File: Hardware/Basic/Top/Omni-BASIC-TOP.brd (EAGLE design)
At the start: 38 x 38 mm, 29 parts, among them U2 NRF52832_MODULE_MDBT42

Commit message: commit operation
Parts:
- added C2, C5, C6: 1u, LinnesLab-Passives:C0603
- added C20, C21: 4.7u, LinnesLab-Passives:C0603
- added C22: 100n, LinnesLab-Passives:C0603
- added C23, C24: 47p, LinnesLab-Passives:C0603
- added CHRG2: MCP73831, LinnesLab-Power:SOT23-5
- added D4, D5: (no value), LinnesLab-DiscreteSemi:USC
- added J1: (no value), LinnesLab-Connectors:1X07
- added J2: (no value), LinnesLab-Connectors:1X02
- added JP2: (no value), LinnesLab-Switches:SMT-JUMPER_2_NO_SILK
- added LDO2: MIC5504, LinnesLab-Power:SOT23-5
- added LED5: RED, LinnesLab-LED:LED-0603
- added LED6: YELLOW, LinnesLab-LED:LED-0603
- added R1, R2: 10k, LinnesLab-Passives:R0603
- added R11: (no value), LinnesLab-Passives:R0603
- added R12, R13, R14, R15: 100k, LinnesLab-Passives:R0603
- added R17, R18: 27, LinnesLab-Passives:R0603
- added R19, R20: 1k, LinnesLab-Passives:R0603
- added R21, R22: 0, LinnesLab-Passives:R0603
- added SW1, SW2: SWITCH.MOM, LinnesLab-Switches:TACTILE_SWITCH_SMD_6.2MM_TALL
- added U4: PCF8523, LinnesLab-Clocks:SO8
- added U5: FT231XS, LinnesLab-DigitalIC:SSOP20_L
- added USB2: USB.MICRO-BIGGERPADS, LinnesLab-Connectors:USB-MICRO-01.BIGGERPADS
- added XTAL3: 32.7680kHz, LinnesLab-Clocks:2-SMD.NOLEAD.2.0MMTO1.2MM
- moved SD2 14.5 mm to (20.3, 14.0), flipped to the bottom, turned to 270 degrees
- moved R7 4.58 mm to (6.58, 13.2)
- moved R6 4.58 mm to (6.58, 15.9)
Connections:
- removed net CD1: SD2.CD1
- removed net CS.OLED: U3.13
- removed net DC.OLED: U3.15
- removed net RESET.OLED: U3.14
- removed net RXD: U2.21
- removed net SD.CS: SD2.2
- removed net TXD: U2.19
- new net !CTS: JP2.2, U5.9
- new net !DTR: U5.1
- new net A4/BATTERY_STATUS: R13.1, R14.2, U2.5
- new net A6/TIA: J1.5, U2.7
- new net A7/PPG: J1.7, U2.8
- new net D11/SW1: SW1.A1, U2.25
- new net D15/SW2: SW2.A1, U2.29
- new net D16/CS.OLED: U2.30, U3.13
- new net D27/CHARGE_STATUS: CHRG2.1, R12.1, U2.4
- new net D29/LED.CONTROL: J1.6, U2.6
- new net D3/RESET.OLED: U2.16, U3.14
- new net D4/DC.OLED: U2.17, U3.15
- new net D5/CD1: SD2.CD1, U2.18
- new net D7/SD.CS: SD2.2, U2.20
- new net FT3V3: U5.13
- new net N$17: CHRG2.5, R11.2
- new net N$19: U4.2, XTAL3.P$1
- new net N$20: U4.1, XTAL3.P$2
- new net N$23: R17.2, U5.12
- new net N$24: R18.2, U5.11
- new net N$25: LED5.C, R19.2
- new net N$26: LED6.C, R20.2
- new net RXD.FT: R22.1, U5.4
- new net RXD.NRF: R21.2, U2.21
- new net RXLED: R19.1, U5.17
- new net TXD.FT: R21.1, U5.20
- new net TXD.NRF: R22.2, U2.19
- new net TXLED: R20.1, U5.10
- new net USB+: C23.1, R18.1, USB2.3
- new net USB-: C24.2, R17.1, USB2.2
- new net VBATT: U4.3
- new net VIN: C21.2, C5.2, CHRG2.4, D4.-, D5.-, LDO2.1, LDO2.3, R12.2
- new net VLIPO: C20.1, CHRG2.3, D4.+, J2.2, R13.2
- new net V_USB: D5.+, U5.15, USB2.1
- net 3.3V: now also C2.1, C22.2, C6.1, LDO2.5, LED5.A, LED6.A, R1.2, R15.2, R2.2, U4.8, U5.14, U5.3
- net GND: now also C2.2, C20.2, C21.1, C22.1, C23.2, C24.1, C5.1, C6.2, CHRG2.2, J2.1, JP2.1, LDO2.2, R11.1, R14.1, R15.1, SW1.B1, SW1.B2, SW2.B1, SW2.B2, U4.4, U5.16, U5.6, USB2.5
- net SCL: now also R2.1, U4.6
- net SDA: now also R1.1, U4.5

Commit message: Latest Update
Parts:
- removed C15: 2.2uF, LinnesLab-Passives:C0402
- removed C2, C6, C7: 1u, LinnesLab-Passives:C0603
- removed C22: 100n, LinnesLab-Passives:C0603
- removed C23, C24: 47p, LinnesLab-Passives:C0603
- removed CHRG2: MCP73831, LinnesLab-Power:SOT23-5
- removed CORTEX1: CORTEX_DEBUG_PTH, LinnesLab-Connectors:2X5-PTH-1.27MM
- removed D4, D5: (no value), LinnesLab-DiscreteSemi:USC
- removed JP2: (no value), LinnesLab-Switches:SMT-JUMPER_2_NO_SILK
- removed L2: 10u, LinnesLab-Passives:L0603
- removed LDO2: MIC5504, LinnesLab-Power:SOT23-5
- removed LED5: RED, LinnesLab-LED:LED-0603
- removed LED6: YELLOW, LinnesLab-LED:LED-0603
- removed R19, R20, R3, R4: 1k, LinnesLab-Passives:R0603
- removed R21, R22: 0, LinnesLab-Passives:R0603
- removed R5: 10k, LinnesLab-Passives:R0603
- removed U2: NRF52832_MODULE_MDBT42, LinnesLab-Microcontrollers:BLE_MODULE_RAYTAC_MDBT42
- removed U5: FT231XS, LinnesLab-DigitalIC:SSOP20_L
- removed USB2: USB.MICRO-BIGGERPADS, LinnesLab-Connectors:USB-MICRO-01.BIGGERPADS
- removed XTAL2: 32.768kHz, LinnesLab-Clocks:2-SMD.NOLEAD.2.0MMTO1.2MM
- removed XTAL3: 32.7680kHz, LinnesLab-Clocks:2-SMD.NOLEAD.2.0MMTO1.2MM
- added C3: 1u, LinnesLab-Passives:C0603
- added C4: 10u, LinnesLab-Passives:C0805
- added D2, D3: (no value), LinnesLab-DiscreteSemi:USC
- added DEBUG1: CORTEX_DEBUG_PTH, LinnesLab-Connectors:2X5-PTH-1.27MM
- added JP1: (no value), LinnesLab-Switches:SMT-JUMPER_2_NO_SILK
- added L1: 10u, LinnesLab-Passives:L0603
- added LED1: RED, LinnesLab-LED:LED-0603
- added LED2: BLUE, LinnesLab-LED:LED-0603
- added R10: 10k, LinnesLab-Passives:R0603
- added R16, R8, R9: 1k, LinnesLab-Passives:R0603
- added U1: NRF52832_MODULE_MDBT42, LinnesLab-Microcontrollers:BLE_MODULE_RAYTAC_MDBT42
- added USB1: USB.MICRO-BIGGERPADS, LinnesLab-Connectors:USB-MICRO-01.BIGGERPADS
- added XTAL1: 32.768kHz, LinnesLab-Clocks:2-SMD.NOLEAD.2.0MMTO1.2MM
- C11: value 300p -> 47p
- C12: value 10u -> 100n; device LinnesLab-Passives:C0805 -> LinnesLab-Passives:C0603
- C13: value 2.2uF -> 47p; device LinnesLab-Passives:C0402 -> LinnesLab-Passives:C0603
- C20, C21: value 4.7u -> 2.2uF; device LinnesLab-Passives:C0603 -> LinnesLab-Passives:C0402
- C5: value 1u -> (none)
- C9: value (none) -> 300p
- J1: device LinnesLab-Connectors:1X07 -> LinnesLab-Connectors:1X02
- J2: device LinnesLab-Connectors:1X02 -> LinnesLab-Connectors:1X07_1.27MM
- LED4: value BLUE -> YELLOW
- R11: value (none) -> 27
- R12: value 100k -> 27
- R13: value 100k -> 10k
- R14: value 100k -> 1k
- R15: value 100k -> 390k
- R17, R18: value 27 -> 0
- R6: value 10k -> 100k
- R7: value 390k -> 100k
- SW1, SW2: value SWITCH.MOM -> (none); device LinnesLab-Switches:TACTILE_SWITCH_SMD_6.2MM_TALL -> LinnesLab-Switches:BUTTON-GULLWING
- SW3, SW4: value (none) -> SWITCH.MOM; device LinnesLab-Switches:BUTTON-GULLWING -> LinnesLab-Switches:TACTILE_SWITCH_SMD_6.2MM_TALL
- U3: value (none) -> FT231XS; device LinnesLab-Displays:UG-2864HSWEG01_0.96IN_NO-WRAPAROUND -> LinnesLab-DigitalIC:SSOP20_L
- U4: value PCF8523 -> (none); device LinnesLab-Clocks:SO8 -> LinnesLab-Displays:UG-2864HSWEG01_0.96IN_NO-WRAPAROUND
- moved R2 62.6 mm to (11.5, 36.4)
- moved R1 58.2 mm to (7.89, 36.3)
- moved R18 50.7 mm to (3.51, 11.3)
- moved C14 49.5 mm to (1.62, 9.02)
- moved R17 46.0 mm to (7.56, 11.3)
- moved D1 43.0 mm to (7.55, 3.31), flipped to the bottom, turned to 270 degrees
- moved SW2 38.9 mm to (35.0, 18.5), turned to 180 degrees
- moved LED4 35.0 mm to (13.5, 9.06), turned to 180 degrees
- moved LED3 34.3 mm to (13.5, 7.64), turned to 180 degrees
- moved SW1 32.0 mm to (35.0, 35.8)
- moved SW3 31.2 mm to (32.2, 3.96), turned to 180 degrees
- moved C11 26.1 mm to (12.5, 5.19), turned to 270 degrees
- moved C13 24.3 mm to (12.2, 1.54), turned to 0 degrees
- moved SW4 24.3 mm to (22.5, 3.96)
- moved C5 21.0 mm to (26.4, 19.4), turned to 180 degrees
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- renumbered SD2 to SD1
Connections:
- removed net N$17: CHRG2.5, R11.2
- removed net N$19: U4.2, XTAL3.P$1
- removed net N$20: U4.1, XTAL3.P$2
- removed net VBATT: U4.3
- net !CTS: now also JP1.2, U3.9; no longer JP2.2, U5.9
- net !DTR: now also U3.1; no longer U5.1
- net 3.3V: now also C14.2, C20.2, C21.2, C4.2, D3.-, DEBUG1.1, J2.4, LED3.A, LED4.A, R10.2, U1.11, U3.14, U3.3, U4.6, U4.9; no longer C12.2, C17.2, C19.2, C2.1, C22.2, C6.1, CORTEX1.1, D1.-, LDO2.5, LED5.A, LED6.A, R15.2, R5.2, U2.11, U3.6, U3.9, U4.8, U5.14, U5.3
- net A4/BATTERY_STATUS: now also R6.1, R7.2, U1.5; no longer R13.1, R14.2, U2.5
- net A6/TIA: now also J2.6, U1.7; no longer J1.5, U2.7
- net A7/PPG: now also J2.7, U1.8; no longer J1.7, U2.8
- net D11/SW1: now also SW3.A1, U1.25; no longer SW1.A1, U2.25
- net D15/SW2: now also SW4.A1, U1.29; no longer SW2.A1, U2.29
- net D16/CS.OLED: now also U1.30, U4.13; no longer U2.30, U3.13
- net D27/CHARGE_STATUS: now also U1.4; no longer CHRG2.1, R12.1, U2.4
- net D29/LED.CONTROL: now also J2.5, U1.6; no longer J1.6, U2.6
- net D3/RESET.OLED: now also U1.16, U4.14; no longer U2.16, U3.14
- net D4/DC.OLED: now also U1.17, U4.15; no longer U2.17, U3.15
- net D5/CD1: now also U1.18; no longer U2.18
- net D7/SD.CS: now also U1.20; no longer U2.20
- net DFU: now also SW1.3, U1.34; no longer SW3.3, U2.34
- net DTR: now also C12.1; no longer C14.1
- net FRST: now also U1.38; no longer U2.38
- net FT3V3: now also U3.13; no longer U5.13
- net GND: now also C11.1, C13.2, C14.1, C20.1, C3.2, C4.1, C8.2, DEBUG1.3, DEBUG1.5, DEBUG1.7, DEBUG1.9, J1.1, J2.3, JP1.1, LED1.C, LED2.C, R13.1, R15.2, R7.1, SW1.1, SW2.3, SW3.B1, SW4.B1, U1.1, U1.12, U1.24, U1.39, U3.16, U3.6, U4.1, U4.10, U4.12, U4.29, U4.30, U4.8, USB1.5; no longer C11.2, C12.1, C17.1, C19.1, C2.2, C20.2, C22.1, C23.2, C24.1, C6.2, C7.2, C8.1, CHRG2.2, CORTEX1.3, CORTEX1.5, CORTEX1.7, CORTEX1.9, J2.1, JP2.1, LDO2.2, LED3.C, LED4.C, R11.1, R14.1, R15.1, R6.1, R7.2, SW1.B1, SW1.B2, SW2.B1, SW2.B2, SW3.1, SW4.3, U2.1, U2.12, U2.24, U2.39, U3.1, U3.10, U3.12, U3.29, U3.30, U3.8, U4.4, U5.16, U5.6, USB2.5
- net LED1: now also R8.2, U1.31; no longer R3.2, U2.31
- net LED2: now also R9.2, U1.33; no longer R4.2, U2.33
- net MISO: now also U1.28; no longer U2.28
- net MOSI: now also U1.27, U4.19; no longer U2.27, U3.19
- net N$1: now also R13.2, U4.11; no longer R6.2, U3.11
- net N$10: now also LED2.A, R9.1; no longer LED4.A, R4.1
- net N$11: now also L1.1, U1.10; no longer L2.1, U2.10
- net N$12: now also C3.1, L1.2, U1.9; no longer C7.1, L2.2, U2.9
- net N$13: now also U4.28; no longer U3.28
- net N$14: now also DEBUG1.8; no longer CORTEX1.8
- net N$15: now also U4.27; no longer U3.27
- net N$2: now also R15.1, U4.26; no longer R7.1, U3.26
- net N$23: now also R11.2, U3.12; no longer R17.2, U5.12
- net N$24: now also R12.2, U3.11; no longer R18.2, U5.11
- net N$25: now also LED3.C, R14.2; no longer LED5.C, R19.2
- net N$26: now also LED4.C, R16.2; no longer LED6.C, R20.2
- net N$3: now also C19.2, U4.2; no longer C13.2, U3.2
- net N$4: now also C5.2, U1.13, XTAL1.P$1; no longer C8.2, U2.13, XTAL2.P$1
- net N$5: now also C19.1, U4.3; no longer C13.1, U3.3
- net N$6: now also C8.1, U1.14, XTAL1.P$2; no longer C9.1, U2.14, XTAL2.P$2
- net N$7: now also C17.2, U4.4; no longer C15.2, U3.4
- net N$8: now also C17.1, U4.5; no longer C15.1, U3.5
- net N$9: now also LED1.A, R8.1; no longer LED3.A, R3.1
- net P0.09/NFC1: now also C9.1, U1.22; no longer C11.1, U2.22
- net P0.10/NFC2: now also U1.23; no longer U2.23
- net RESET: now also C12.2, D3.+, DEBUG1.10, R10.1, SW2.1, U1.35; no longer C14.2, CORTEX1.10, D1.+, R5.1, SW4.1, U2.35
- net RXD.FT: now also R18.1, U3.4; no longer R22.1, U5.4
- net RXD.NRF: now also R17.2, U1.21; no longer R21.2, U2.21
- net RXLED: now also R14.1, U3.17; no longer R19.1, U5.17
- net SCK: now also U1.26, U4.18; no longer U2.26, U3.18
- net SCL: now also J2.2, U1.3; no longer U2.3, U4.6
- net SDA: now also J2.1, U1.2; no longer U2.2, U4.5
- net SWCLK: now also DEBUG1.4, U1.36; no longer CORTEX1.4, U2.36
- net SWDIO: now also DEBUG1.2, U1.37; no longer CORTEX1.2, U2.37
- net SWO: now also DEBUG1.6, U1.32; no longer CORTEX1.6, U2.32
- net TXD.FT: now also R17.1, U3.20; no longer R21.1, U5.20
- net TXD.NRF: now also R18.2, U1.19; no longer R22.2, U2.19
- net TXLED: now also R16.1, U3.10; no longer R20.1, U5.10
- net USB+: now also C13.1, R12.1, USB1.3; no longer C23.1, R18.1, USB2.3
- net USB-: now also C11.2, R11.1, USB1.2; no longer C24.2, R17.1, USB2.2
- net VIN: now also D1.-, D2.-; no longer C21.2, C5.2, CHRG2.4, D4.-, D5.-, LDO2.1, LDO2.3, R12.2
- net VLIPO: now also D1.+, J1.2, R6.2; no longer C20.1, CHRG2.3, D4.+, J2.2, R13.2
- net V_USB: now also D2.+, U3.15, USB1.1; no longer D5.+, U5.15, USB2.1
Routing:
- net GND: track 0.00 -> 33.0 mm, vias 0 -> 18
- net TXLED: track 0.00 -> 26.3 mm, vias 0 -> 2
- net VLIPO: track 0.00 -> 17.8 mm
- net USB+: track 0.00 -> 12.4 mm, vias 0 -> 1
- net USB-: track 0.00 -> 11.4 mm, vias 0 -> 1
- net N$2: track 0.00 -> 8.55 mm
- net LED2: track 0.00 -> 6.95 mm
- net N$6: track 0.00 -> 5.66 mm
- net RXD.FT: track 0.00 -> 5.19 mm
- net N$13: track 0.00 -> 4.52 mm
- net LED1: track 0.00 -> 4.22 mm
- net N$12: track 0.00 -> 3.78 mm
- net N$4: track 0.00 -> 3.58 mm
- net N$8: track 0.00 -> 3.22 mm
- net N$5: track 0.00 -> 3.22 mm
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- added copper zone on layer 1, net 3.3V
- added copper zone on layer 16, net GND

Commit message: End of class update
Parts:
- moved SW3 9.79 mm to (22.4, 4.03)
- moved SW4 9.60 mm to (32.1, 4.03)
- moved LED1 3.70 mm to (32.8, 21.7)
- moved XTAL1 2.63 mm to (22.5, 20.6)
- moved C18 2.52 mm to (20.0, 20.6)
- moved U1 2.43 mm to (25.0, 29.9)
- moved C3 2.32 mm to (18.7, 28.9)
- moved L1 2.30 mm to (18.6, 25.9)
- moved R10 1.91 mm to (34.4, 15.0)
- moved C12 1.88 mm to (34.6, 12.3)
- moved D3 1.82 mm to (34.6, 13.5)
- moved DEBUG1 1.43 mm to (34.9, 30.3)
- moved SD1 1.38 mm to (20.3, 15.4)
- moved R8 1.38 mm to (33.1, 24.6)
- moved R9 1.36 mm to (35.1, 24.3)
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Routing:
- net RESET: track 0.00 -> 28.3 mm, vias 0 -> 1
- net D15/SW2: track 0.00 -> 23.7 mm, vias 0 -> 2
- net D16/CS.OLED: track 0.00 -> 22.3 mm, vias 0 -> 2
- net D11/SW1: track 0.00 -> 19.6 mm
- net MOSI: track 0.00 -> 18.5 mm, vias 0 -> 2
- net D3/RESET.OLED: track 0.00 -> 17.8 mm, vias 0 -> 2
- net SCK: track 0.00 -> 16.8 mm, vias 0 -> 2
- net DFU: track 0.00 -> 14.5 mm, vias 0 -> 3
- net D4/DC.OLED: track 0.00 -> 14.3 mm, vias 0 -> 2
- net SWO: track 0.00 -> 11.3 mm, vias 0 -> 1
- net SWCLK: track 0.00 -> 10.4 mm
- net SWDIO: track 0.00 -> 6.83 mm, vias 0 -> 1
- net GND: track 33.0 -> 38.0 mm, vias 18 -> 22
- net N$4: track 3.58 -> 6.25 mm
- net !CTS: track 0.00 -> 2.39 mm
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
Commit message: Update 2703-1
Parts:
- moved C4 10.2 mm to (15.9, 29.0), turned to 0 degrees
- moved R2 8.91 mm to (3.61, 32.2), turned to 270 degrees
- moved R1 6.97 mm to (2.21, 32.2), turned to 270 degrees
- moved C3 2.82 mm to (16.4, 27.4), turned to 180 degrees
- moved L1 1.34 mm to (17.3, 26.1), turned to 0 degrees
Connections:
- removed net A4/BATTERY_STATUS: R6.1, R7.2, U1.5
- removed net A6/TIA: J2.6, U1.7
- removed net A7/PPG: J2.7, U1.8
- removed net D29/LED.CONTROL: J2.5, U1.6
- new net A4/PPG: J2.7, U1.5
- new net A5/TIA: J2.6, U1.6
- new net A7/BATTERY_STATUS: R6.1, R7.2, U1.8
- new net D30/LED_CONTROL: J2.5, U1.7
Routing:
- net RXD.NRF: track 0.00 -> 25.0 mm, vias 0 -> 2
- net A7/BATTERY_STATUS: track 0.00 -> 24.5 mm, vias 0 -> 2
- net MOSI: track 18.5 -> 0.04 mm, vias 2 -> 0
- net SDA: track 0.00 -> 17.3 mm, vias 0 -> 1
- net SCL: track 0.00 -> 16.6 mm, vias 0 -> 1
- net A5/TIA: track 0.00 -> 13.6 mm, vias 0 -> 1
- net D30/LED_CONTROL: track 0.00 -> 12.8 mm, vias 0 -> 1
- net A4/PPG: track 0.00 -> 9.65 mm, vias 0 -> 1
- net GND: track 38.0 -> 42.7 mm, vias 22 -> 24
- net N$11: track 1.85 -> 4.48 mm
- net N$12: track 3.57 -> 4.11 mm

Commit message: End of class update
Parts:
- removed C10, C9: 300p, LinnesLab-Passives:C0603
- removed SD1: (no value), LinnesLab-Connectors:MICROSD
- moved R18 13.0 mm to (16.5, 11.1)
- moved R17 9.04 mm to (16.5, 9.75)
- moved C13 1.23 mm to (13.4, 1.91)
- moved JP1 0.38 mm to (2.33, 2.20)
- moved SW1 0.36 mm to (35.0, 35.4)
- moved J1 0.23 mm to (2.42, 15.8)
- moved DEBUG1 0.09 mm to (34.9, 30.3)
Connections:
- removed net !DTR: U3.1
- removed net CD2: SD1.CD2
- net 3.3V: no longer SD1.4
- net D5/CD1: no longer SD1.CD1
- net D7/SD.CS: no longer SD1.2
- net DTR: now also U3.1
- net GND: no longer C10.2, C9.2, SD1.6, SD1.MT1, SD1.MT2
- net MISO: no longer SD1.7
- net MOSI: no longer SD1.3
- net P0.09/NFC1: no longer C9.1
- net P0.10/NFC2: no longer C10.1
- net SCK: no longer SD1.5
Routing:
- net DTR: track 0.00 -> 35.6 mm, vias 0 -> 2
- net TXD.NRF: track 0.00 -> 17.5 mm, vias 0 -> 2
- net MOSI: track 0.04 -> 16.9 mm, vias 0 -> 2
- net GND: track 42.7 -> 57.9 mm, vias 24 -> 23
- net RXD.FT: track 5.19 -> 14.7 mm
- net TXD.FT: track 2.95 -> 9.47 mm
- net RXD.NRF: track 25.0 -> 19.9 mm
- net SCK: track 16.9 -> 20.9 mm
- net SDA: track 17.3 -> 20.7 mm
- net SCL: track 16.6 -> 19.4 mm
- net V_USB: track 1.80 -> 4.58 mm, vias 0 -> 1
- net D4/DC.OLED: track 14.7 -> 16.5 mm
- net USB+: track 12.4 -> 13.8 mm
- net 3.3V: track 0.32 -> 1.74 mm
- net D15/SW2: track 23.8 -> 25.1 mm
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
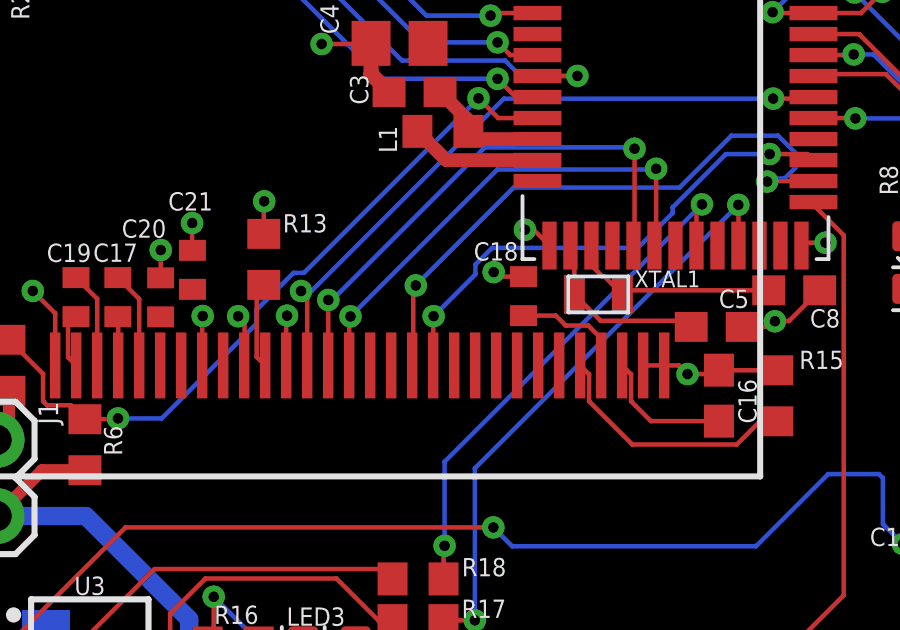
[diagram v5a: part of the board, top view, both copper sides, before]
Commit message: Fixed 1 of 2 airwires update
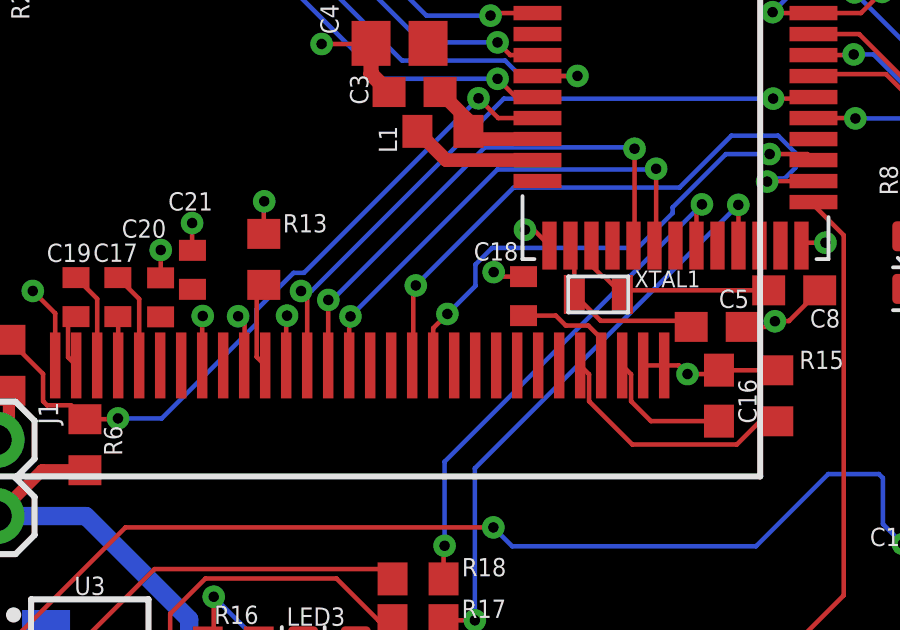
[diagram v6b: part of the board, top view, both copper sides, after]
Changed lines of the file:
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@@
 <wire x1="15.2679375" y1="1.910078125" x2="15.318740625" y2="1.96088125" width="0.1524" layer="1"/>
 <via x="15.318740625" y="1.96088125" extent="1-16" drill="0.35"/>
-<wire x1="20.849478125" y1="22.2483375" x2="19.984725" y2="21.21384375" width="0" layer="19" extent="1-1"/>
 <wire x1="13.522959375" y1="6.0706" x2="14.220559375" y2="1.910078125" width="0" layer="19" extent="1-1"/>
 </signal>
@@
 <contactref element="U1" pad="27"/>
 <contactref element="U4" pad="19"/>
-<wire x1="16.97371875" y1="18.253859375" x2="16.97371875" y2="19.88201875" width="0.1524" layer="1"/>
-<wire x1="16.97371875" y1="19.88201875" x2="16.98751875" y2="19.89581875" width="0.1524" layer="1"/>
-<via x="16.98751875" y="19.89581875" extent="1-16" drill="0.35"/>
+<wire x1="16.97371875" y1="18.253859375" x2="16.97371875" y2="19.4959375" width="0.1524" layer="1"/>
+<wire x1="16.97371875" y1="19.4959375" x2="17.447259375" y2="19.969478125" width="0.1524" layer="1"/>
+<via x="17.447259375" y="19.969478125" extent="1-16" drill="0.35"/>
 <via x="28.18891875" y="25.2984" extent="1-16" drill="0.35"/>
-<wire x1="16.98751875" y1="19.89581875" x2="18.38224375" y2="21.29054375" width="0.1524" layer="16"/>
-<wire x1="18.38224375" y1="21.29054375" x2="18.38224375" y2="21.6152875" width="0.1524" layer="16"/>
+<wire x1="17.447259375" y1="19.969478125" x2="18.38224375" y2="20.9044625" width="0.1524" layer="16"/>
+<wire x1="18.38224375" y1="20.9044625" x2="18.38224375" y2="21.6152875" width="0.1524" layer="16"/>
 <wire x1="18.38224375" y1="21.6152875" x2="18.9363375" y2="22.16938125" width="0.1524" layer="16"/>
 <wire x1="18.9363375" y1="22.16938125" x2="23.7919125" y2="22.16938125" width="0.1524" layer="16"/>
